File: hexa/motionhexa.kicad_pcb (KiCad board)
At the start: 2 copper layers, 64 x 55.4 mm, 173 parts, among them J1 Conn_01x13_Socket, J2 Conn_01x13_Socket

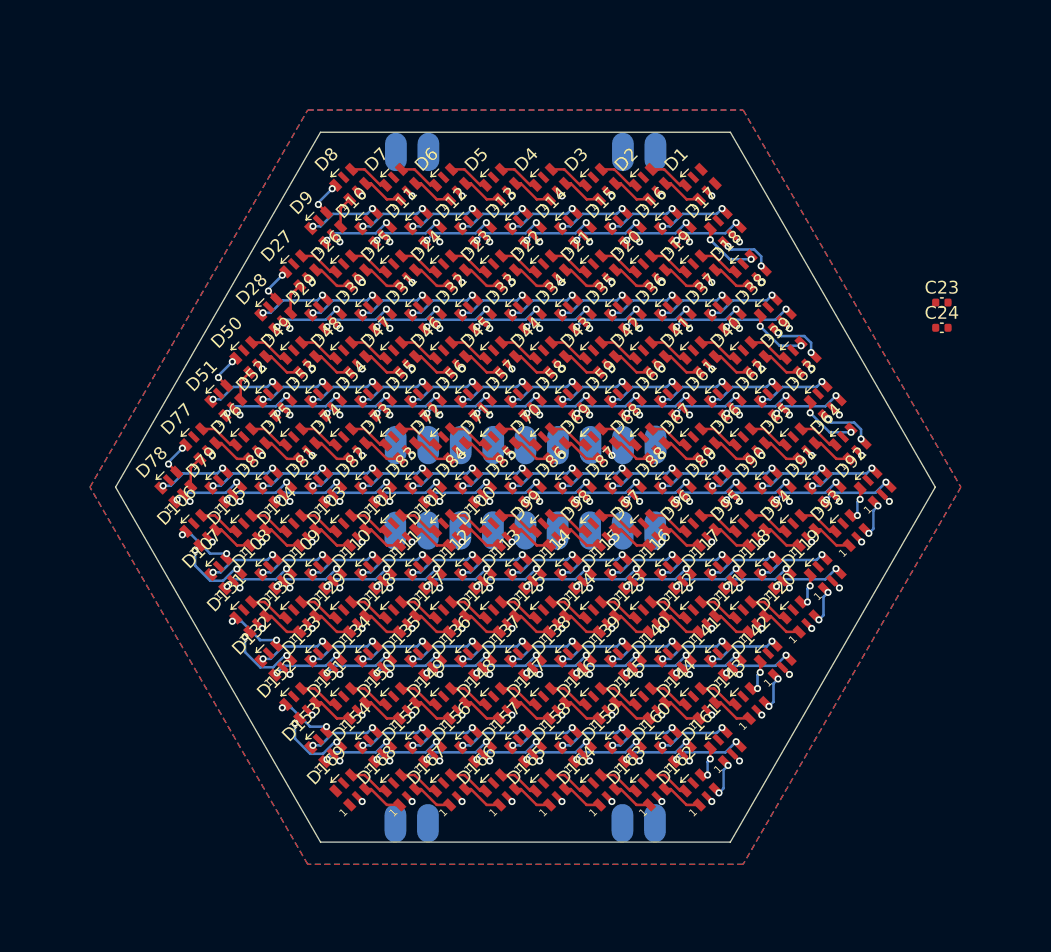
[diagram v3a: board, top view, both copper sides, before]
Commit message: flip direction of pixel data flow and redo all the traces; improvements to layout script including using TraceBuilder for gnd and power draws, and a --lock cli option
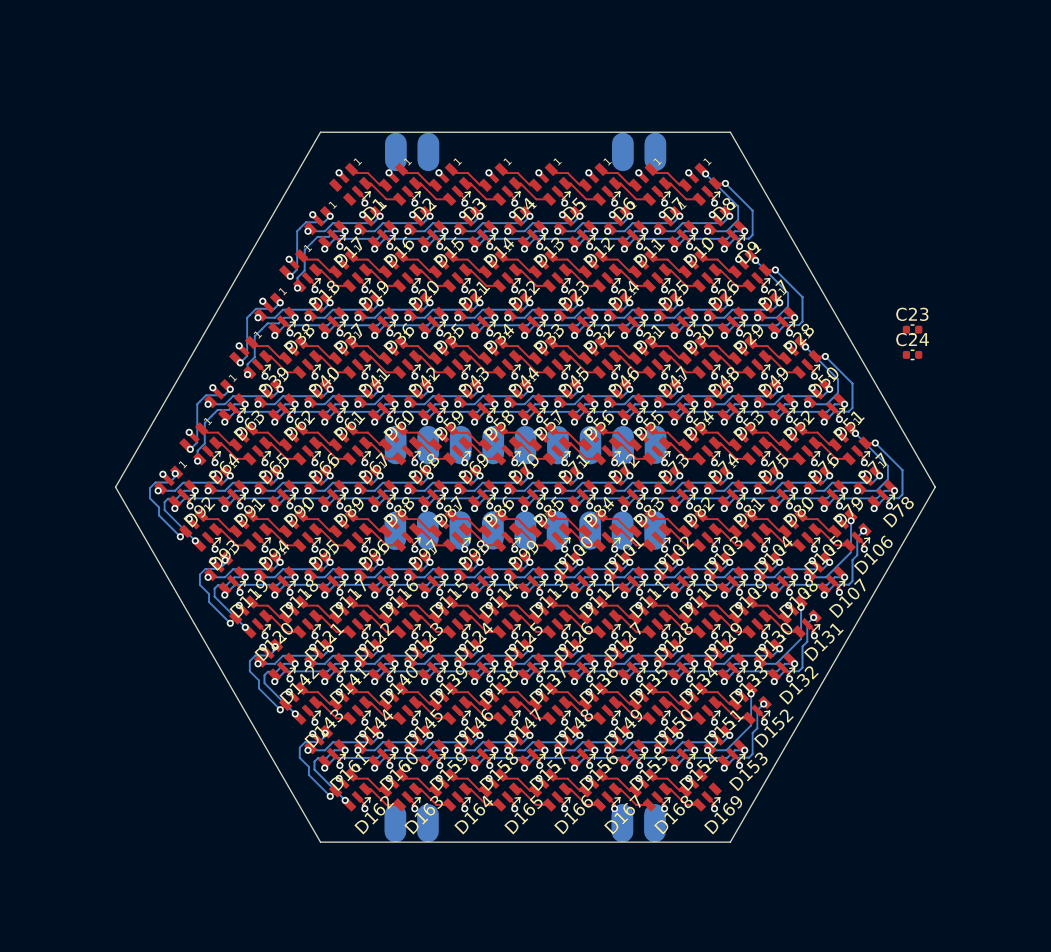
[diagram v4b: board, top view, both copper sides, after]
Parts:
- moved D78 54.6 mm to (127.3, 100.0), turned to 45 degrees
- moved D92 54.6 mm to (72.7, 100.0), turned to 45 degrees
- moved D106 50.7 mm to (125.3, 103.4), turned to 45 degrees
- moved D64 50.7 mm to (74.7, 96.6), turned to 45 degrees
- moved D77 50.7 mm to (125.3, 96.6), turned to 45 degrees
- moved D93 50.7 mm to (74.7, 103.4), turned to 45 degrees
- moved D107 46.8 mm to (123.4, 106.8), turned to 45 degrees
- moved D119 46.8 mm to (76.6, 106.8), turned to 45 degrees
- moved D51 46.8 mm to (123.4, 93.2), turned to 45 degrees
- moved D63 46.8 mm to (76.6, 93.2), turned to 45 degrees
- moved D79 46.8 mm to (123.4, 100.0), turned to 45 degrees
- moved D91 46.8 mm to (76.6, 100.0), turned to 45 degrees
- moved D105 42.9 mm to (121.5, 103.4), turned to 45 degrees
- moved D131 42.9 mm to (121.5, 110.1), turned to 45 degrees
- moved D50 42.9 mm to (121.5, 89.9), turned to 45 degrees
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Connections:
- D1 pad 1: (no net) -> Net-(D1-SDO)
- D1 pad 3: (no net) -> SPI_TX
- D1 pad 4: (no net) -> SPI_SCK
- D1 pad 6: (no net) -> Net-(D1-CKO)
- D10 pad 1: (no net) -> Net-(D10-SDO)
- D10 pad 6: (no net) -> Net-(D10-CKO)
- D100 pad 1: (no net) -> Net-(D100-SDO)
- D100 pad 6: (no net) -> Net-(D100-CKO)
- D101 pad 1: (no net) -> Net-(D101-SDO)
- D101 pad 6: (no net) -> Net-(D101-CKO)
- D102 pad 1: (no net) -> Net-(D102-SDO)
- D102 pad 6: (no net) -> Net-(D102-CKO)
- D103 pad 1: (no net) -> Net-(D103-SDO)
- D103 pad 6: (no net) -> Net-(D103-CKO)
- D104 pad 1: (no net) -> Net-(D104-SDO)
- D104 pad 6: (no net) -> Net-(D104-CKO)
- D105 pad 1: (no net) -> Net-(D105-SDO)
- D105 pad 6: (no net) -> Net-(D105-CKO)
- D106 pad 1: (no net) -> Net-(D106-SDO)
- D106 pad 6: (no net) -> Net-(D106-CKO)
- D107 pad 1: (no net) -> Net-(D107-SDO)
- D107 pad 6: (no net) -> Net-(D107-CKO)
- D108 pad 1: (no net) -> Net-(D108-SDO)
- D108 pad 6: (no net) -> Net-(D108-CKO)
- D109 pad 1: (no net) -> Net-(D109-SDO)
- D109 pad 6: (no net) -> Net-(D109-CKO)
- D11 pad 1: (no net) -> Net-(D11-SDO)
- D11 pad 6: (no net) -> Net-(D11-CKO)
- D110 pad 1: (no net) -> Net-(D110-SDO)
- D110 pad 6: (no net) -> Net-(D110-CKO)
- D111 pad 1: (no net) -> Net-(D111-SDO)
- D111 pad 6: (no net) -> Net-(D111-CKO)
- D112 pad 1: (no net) -> Net-(D112-SDO)
- D112 pad 6: (no net) -> Net-(D112-CKO)
- D113 pad 1: (no net) -> Net-(D113-SDO)
- D113 pad 6: (no net) -> Net-(D113-CKO)
- D114 pad 1: (no net) -> Net-(D114-SDO)
- D114 pad 6: (no net) -> Net-(D114-CKO)
- D115 pad 1: (no net) -> Net-(D115-SDO)
- D115 pad 6: (no net) -> Net-(D115-CKO)
- D116 pad 1: (no net) -> Net-(D116-SDO)
- D116 pad 6: (no net) -> Net-(D116-CKO)
- D117 pad 1: (no net) -> Net-(D117-SDO)
- D117 pad 6: (no net) -> Net-(D117-CKO)
- D118 pad 1: (no net) -> Net-(D118-SDO)
- D118 pad 6: (no net) -> Net-(D118-CKO)
- D119 pad 1: (no net) -> Net-(D119-SDO)
- D119 pad 6: (no net) -> Net-(D119-CKO)
- D12 pad 1: (no net) -> Net-(D12-SDO)
- D12 pad 6: (no net) -> Net-(D12-CKO)
- D120 pad 1: (no net) -> Net-(D120-SDO)
- D120 pad 6: (no net) -> Net-(D120-CKO)
- D121 pad 1: (no net) -> Net-(D121-SDO)
- D121 pad 6: (no net) -> Net-(D121-CKO)
- D122 pad 1: (no net) -> Net-(D122-SDO)
- D122 pad 6: (no net) -> Net-(D122-CKO)
- D123 pad 1: (no net) -> Net-(D123-SDO)
- D123 pad 6: (no net) -> Net-(D123-CKO)
- D124 pad 1: (no net) -> Net-(D124-SDO)
- D124 pad 6: (no net) -> Net-(D124-CKO)
- D125 pad 1: (no net) -> Net-(D125-SDO)
- D125 pad 6: (no net) -> Net-(D125-CKO)
- D126 pad 1: (no net) -> Net-(D126-SDO)
- D126 pad 6: (no net) -> Net-(D126-CKO)
- D127 pad 1: (no net) -> Net-(D127-SDO)
- D127 pad 6: (no net) -> Net-(D127-CKO)
- D128 pad 1: (no net) -> Net-(D128-SDO)
- D128 pad 6: (no net) -> Net-(D128-CKO)
- D129 pad 1: (no net) -> Net-(D129-SDO)
- D129 pad 6: (no net) -> Net-(D129-CKO)
- D13 pad 1: (no net) -> Net-(D13-SDO)
- D13 pad 6: (no net) -> Net-(D13-CKO)
- D130 pad 1: (no net) -> Net-(D130-SDO)
- D130 pad 6: (no net) -> Net-(D130-CKO)
- D131 pad 1: (no net) -> Net-(D131-SDO)
- D131 pad 6: (no net) -> Net-(D131-CKO)
- D132 pad 1: (no net) -> Net-(D132-SDO)
- D132 pad 6: (no net) -> Net-(D132-CKO)
- D133 pad 1: (no net) -> Net-(D133-SDO)
- D133 pad 6: (no net) -> Net-(D133-CKO)
- D134 pad 1: (no net) -> Net-(D134-SDO)
- D134 pad 6: (no net) -> Net-(D134-CKO)
- D135 pad 1: (no net) -> Net-(D135-SDO)
- D135 pad 6: (no net) -> Net-(D135-CKO)
- D136 pad 1: (no net) -> Net-(D136-SDO)
- D136 pad 6: (no net) -> Net-(D136-CKO)
- D137 pad 1: (no net) -> Net-(D137-SDO)
- D137 pad 6: (no net) -> Net-(D137-CKO)
- D138 pad 1: (no net) -> Net-(D138-SDO)
- D138 pad 6: (no net) -> Net-(D138-CKO)
- D139 pad 1: (no net) -> Net-(D139-SDO)
- D139 pad 6: (no net) -> Net-(D139-CKO)
- D14 pad 1: (no net) -> Net-(D14-SDO)
- D14 pad 6: (no net) -> Net-(D14-CKO)
- D140 pad 1: (no net) -> Net-(D140-SDO)
- D140 pad 6: (no net) -> Net-(D140-CKO)
- D141 pad 1: (no net) -> Net-(D141-SDO)
- D141 pad 6: (no net) -> Net-(D141-CKO)
- D142 pad 1: (no net) -> Net-(D142-SDO)
- D142 pad 6: (no net) -> Net-(D142-CKO)
- D143 pad 1: (no net) -> Net-(D143-SDO)
- D143 pad 6: (no net) -> Net-(D143-CKO)
- D144 pad 1: (no net) -> Net-(D144-SDO)
- D144 pad 6: (no net) -> Net-(D144-CKO)
- D145 pad 1: (no net) -> Net-(D145-SDO)
- D145 pad 6: (no net) -> Net-(D145-CKO)
- D146 pad 1: (no net) -> Net-(D146-SDO)
- D146 pad 6: (no net) -> Net-(D146-CKO)
- D147 pad 1: (no net) -> Net-(D147-SDO)
- D147 pad 6: (no net) -> Net-(D147-CKO)
- D148 pad 1: (no net) -> Net-(D148-SDO)
- D148 pad 6: (no net) -> Net-(D148-CKO)
- D149 pad 1: (no net) -> Net-(D149-SDO)
- D149 pad 6: (no net) -> Net-(D149-CKO)
- D15 pad 1: (no net) -> Net-(D15-SDO)
- D15 pad 6: (no net) -> Net-(D15-CKO)
- D150 pad 1: (no net) -> Net-(D150-SDO)
- D150 pad 6: (no net) -> Net-(D150-CKO)
- D151 pad 1: (no net) -> Net-(D151-SDO)
- D151 pad 6: (no net) -> Net-(D151-CKO)
- D152 pad 1: (no net) -> Net-(D152-SDO)
- D152 pad 6: (no net) -> Net-(D152-CKO)
- D153 pad 1: (no net) -> Net-(D153-SDO)
- D153 pad 6: (no net) -> Net-(D153-CKO)
- D154 pad 1: (no net) -> Net-(D154-SDO)
- D154 pad 6: (no net) -> Net-(D154-CKO)
- D155 pad 1: (no net) -> Net-(D155-SDO)
- D155 pad 6: (no net) -> Net-(D155-CKO)
- D156 pad 1: (no net) -> Net-(D156-SDO)
- D156 pad 6: (no net) -> Net-(D156-CKO)
- D157 pad 1: (no net) -> Net-(D157-SDO)
- D157 pad 6: (no net) -> Net-(D157-CKO)
- D158 pad 1: (no net) -> Net-(D158-SDO)
- D158 pad 6: (no net) -> Net-(D158-CKO)
- D159 pad 1: (no net) -> Net-(D159-SDO)
- D159 pad 6: (no net) -> Net-(D159-CKO)
- D16 pad 1: (no net) -> Net-(D16-SDO)
- D16 pad 6: (no net) -> Net-(D16-CKO)
- D160 pad 1: (no net) -> Net-(D160-SDO)
- D160 pad 6: (no net) -> Net-(D160-CKO)
- D161 pad 1: (no net) -> Net-(D161-SDO)
- D161 pad 6: (no net) -> Net-(D161-CKO)
- D162 pad 1: (no net) -> Net-(D162-SDO)
- D162 pad 6: (no net) -> Net-(D162-CKO)
- D163 pad 1: (no net) -> Net-(D163-SDO)
- D163 pad 6: (no net) -> Net-(D163-CKO)
- D164 pad 1: (no net) -> Net-(D164-SDO)
- D164 pad 6: (no net) -> Net-(D164-CKO)
- D165 pad 1: (no net) -> Net-(D165-SDO)
- D165 pad 6: (no net) -> Net-(D165-CKO)
- D166 pad 1: (no net) -> Net-(D166-SDO)
- D166 pad 6: (no net) -> Net-(D166-CKO)
- D167 pad 1: (no net) -> Net-(D167-SDO)
- D167 pad 6: (no net) -> Net-(D167-CKO)
- D168 pad 1: (no net) -> Net-(D168-SDO)
- D168 pad 6: (no net) -> Net-(D168-CKO)
- D169 pad 1: (no net) -> unconnected-(D169-SDO-Pad1)
- D169 pad 6: (no net) -> unconnected-(D169-CKO-Pad6)
- D17 pad 1: (no net) -> Net-(D17-SDO)
- D17 pad 6: (no net) -> Net-(D17-CKO)
- D18 pad 1: (no net) -> Net-(D18-SDO)
- D18 pad 6: (no net) -> Net-(D18-CKO)
- D19 pad 1: (no net) -> Net-(D19-SDO)
- D19 pad 6: (no net) -> Net-(D19-CKO)
- D2 pad 1: (no net) -> Net-(D2-SDO)
- D2 pad 6: (no net) -> Net-(D2-CKO)
- D20 pad 1: (no net) -> Net-(D20-SDO)
- D20 pad 6: (no net) -> Net-(D20-CKO)
- D21 pad 1: (no net) -> Net-(D21-SDO)
- D21 pad 6: (no net) -> Net-(D21-CKO)
- D22 pad 1: (no net) -> Net-(D22-SDO)
- D22 pad 6: (no net) -> Net-(D22-CKO)
- D23 pad 1: (no net) -> Net-(D23-SDO)
- D23 pad 6: (no net) -> Net-(D23-CKO)
- D24 pad 1: (no net) -> Net-(D24-SDO)
- D24 pad 6: (no net) -> Net-(D24-CKO)
- D25 pad 1: (no net) -> Net-(D25-SDO)
- D25 pad 6: (no net) -> Net-(D25-CKO)
- D26 pad 1: (no net) -> Net-(D26-SDO)
- D26 pad 6: (no net) -> Net-(D26-CKO)
- D27 pad 1: (no net) -> Net-(D27-SDO)
- D27 pad 6: (no net) -> Net-(D27-CKO)
- D28 pad 1: (no net) -> Net-(D28-SDO)
- D28 pad 6: (no net) -> Net-(D28-CKO)
- D29 pad 1: (no net) -> Net-(D29-SDO)
- D29 pad 6: (no net) -> Net-(D29-CKO)
- D3 pad 1: (no net) -> Net-(D3-SDO)
- D3 pad 6: (no net) -> Net-(D3-CKO)
- D30 pad 1: (no net) -> Net-(D30-SDO)
- D30 pad 6: (no net) -> Net-(D30-CKO)
- D31 pad 1: (no net) -> Net-(D31-SDO)
- D31 pad 6: (no net) -> Net-(D31-CKO)
- D32 pad 1: (no net) -> Net-(D32-SDO)
- D32 pad 6: (no net) -> Net-(D32-CKO)
- D33 pad 1: (no net) -> Net-(D33-SDO)
- D33 pad 6: (no net) -> Net-(D33-CKO)
- D34 pad 1: (no net) -> Net-(D34-SDO)
- D34 pad 6: (no net) -> Net-(D34-CKO)
- D35 pad 1: (no net) -> Net-(D35-SDO)
- D35 pad 6: (no net) -> Net-(D35-CKO)
- D36 pad 1: (no net) -> Net-(D36-SDO)
- D36 pad 6: (no net) -> Net-(D36-CKO)
- D37 pad 1: (no net) -> Net-(D37-SDO)
- D37 pad 6: (no net) -> Net-(D37-CKO)
- D38 pad 1: (no net) -> Net-(D38-SDO)
- D38 pad 6: (no net) -> Net-(D38-CKO)
- D39 pad 1: (no net) -> Net-(D39-SDO)
- D39 pad 6: (no net) -> Net-(D39-CKO)
- D4 pad 1: (no net) -> Net-(D4-SDO)
- D4 pad 6: (no net) -> Net-(D4-CKO)
- D40 pad 1: (no net) -> Net-(D40-SDO)
- D40 pad 6: (no net) -> Net-(D40-CKO)
- D41 pad 1: (no net) -> Net-(D41-SDO)
- D41 pad 6: (no net) -> Net-(D41-CKO)
- D42 pad 1: (no net) -> Net-(D42-SDO)
- D42 pad 6: (no net) -> Net-(D42-CKO)
- D43 pad 1: (no net) -> Net-(D43-SDO)
- D43 pad 6: (no net) -> Net-(D43-CKO)
- D44 pad 1: (no net) -> Net-(D44-SDO)
- D44 pad 6: (no net) -> Net-(D44-CKO)
- D45 pad 1: (no net) -> Net-(D45-SDO)
- D45 pad 6: (no net) -> Net-(D45-CKO)
- D46 pad 1: (no net) -> Net-(D46-SDO)
- D46 pad 6: (no net) -> Net-(D46-CKO)
- D47 pad 1: (no net) -> Net-(D47-SDO)
- D47 pad 6: (no net) -> Net-(D47-CKO)
- D48 pad 1: (no net) -> Net-(D48-SDO)
- D48 pad 6: (no net) -> Net-(D48-CKO)
- D49 pad 1: (no net) -> Net-(D49-SDO)
- D49 pad 6: (no net) -> Net-(D49-CKO)
- D5 pad 1: (no net) -> Net-(D5-SDO)
- D5 pad 6: (no net) -> Net-(D5-CKO)
- D50 pad 1: (no net) -> Net-(D50-SDO)
- D50 pad 6: (no net) -> Net-(D50-CKO)
- D51 pad 1: (no net) -> Net-(D51-SDO)
- D51 pad 6: (no net) -> Net-(D51-CKO)
- D52 pad 1: (no net) -> Net-(D52-SDO)
- D52 pad 6: (no net) -> Net-(D52-CKO)
- D53 pad 1: (no net) -> Net-(D53-SDO)
- D53 pad 6: (no net) -> Net-(D53-CKO)
- D54 pad 1: (no net) -> Net-(D54-SDO)
- D54 pad 6: (no net) -> Net-(D54-CKO)
- D55 pad 1: (no net) -> Net-(D55-SDO)
- D55 pad 6: (no net) -> Net-(D55-CKO)
- D56 pad 1: (no net) -> Net-(D56-SDO)
- D56 pad 6: (no net) -> Net-(D56-CKO)
- D57 pad 1: (no net) -> Net-(D57-SDO)
- D57 pad 6: (no net) -> Net-(D57-CKO)
- D58 pad 1: (no net) -> Net-(D58-SDO)
- D58 pad 6: (no net) -> Net-(D58-CKO)
- D59 pad 1: (no net) -> Net-(D59-SDO)
- D59 pad 6: (no net) -> Net-(D59-CKO)
- D6 pad 1: (no net) -> Net-(D6-SDO)
- D6 pad 6: (no net) -> Net-(D6-CKO)
- D60 pad 1: (no net) -> Net-(D60-SDO)
- D60 pad 6: (no net) -> Net-(D60-CKO)
- D61 pad 1: (no net) -> Net-(D61-SDO)
- D61 pad 6: (no net) -> Net-(D61-CKO)
- D62 pad 1: (no net) -> Net-(D62-SDO)
- D62 pad 6: (no net) -> Net-(D62-CKO)
- D63 pad 1: (no net) -> Net-(D63-SDO)
- D63 pad 6: (no net) -> Net-(D63-CKO)
- D64 pad 1: (no net) -> Net-(D64-SDO)
- D64 pad 6: (no net) -> Net-(D64-CKO)
- D65 pad 1: (no net) -> Net-(D65-SDO)
- D65 pad 6: (no net) -> Net-(D65-CKO)
- D66 pad 1: (no net) -> Net-(D66-SDO)
- D66 pad 6: (no net) -> Net-(D66-CKO)
- D67 pad 1: (no net) -> Net-(D67-SDO)
- D67 pad 6: (no net) -> Net-(D67-CKO)
- D68 pad 1: (no net) -> Net-(D68-SDO)
- D68 pad 6: (no net) -> Net-(D68-CKO)
- D69 pad 1: (no net) -> Net-(D69-SDO)
- D69 pad 6: (no net) -> Net-(D69-CKO)
- D7 pad 1: (no net) -> Net-(D7-SDO)
- D7 pad 6: (no net) -> Net-(D7-CKO)
- D70 pad 1: (no net) -> Net-(D70-SDO)
- D70 pad 6: (no net) -> Net-(D70-CKO)
- D71 pad 1: (no net) -> Net-(D71-SDO)
- D71 pad 6: (no net) -> Net-(D71-CKO)
- D72 pad 1: (no net) -> Net-(D72-SDO)
- D72 pad 6: (no net) -> Net-(D72-CKO)
- D73 pad 1: (no net) -> Net-(D73-SDO)
- D73 pad 6: (no net) -> Net-(D73-CKO)
- D74 pad 1: (no net) -> Net-(D74-SDO)
- D74 pad 6: (no net) -> Net-(D74-CKO)
- D75 pad 1: (no net) -> Net-(D75-SDO)
- D75 pad 6: (no net) -> Net-(D75-CKO)
- D76 pad 1: (no net) -> Net-(D76-SDO)
- D76 pad 6: (no net) -> Net-(D76-CKO)
- D77 pad 1: (no net) -> Net-(D77-SDO)
- D77 pad 6: (no net) -> Net-(D77-CKO)
- D78 pad 1: (no net) -> Net-(D78-SDO)
- D78 pad 6: (no net) -> Net-(D78-CKO)
- D79 pad 1: (no net) -> Net-(D79-SDO)
- D79 pad 6: (no net) -> Net-(D79-CKO)
- D8 pad 1: (no net) -> Net-(D8-SDO)
- D8 pad 6: (no net) -> Net-(D8-CKO)
- D80 pad 1: (no net) -> Net-(D80-SDO)
- D80 pad 6: (no net) -> Net-(D80-CKO)
- D81 pad 1: (no net) -> Net-(D81-SDO)
- D81 pad 6: (no net) -> Net-(D81-CKO)
- D82 pad 1: (no net) -> Net-(D82-SDO)
- D82 pad 6: (no net) -> Net-(D82-CKO)
- D83 pad 1: (no net) -> Net-(D83-SDO)
- D83 pad 6: (no net) -> Net-(D83-CKO)
- D84 pad 1: (no net) -> Net-(D84-SDO)
- D84 pad 6: (no net) -> Net-(D84-CKO)
- D85 pad 1: (no net) -> Net-(D85-SDO)
- D85 pad 6: (no net) -> Net-(D85-CKO)
- D86 pad 1: (no net) -> Net-(D86-SDO)
- D86 pad 6: (no net) -> Net-(D86-CKO)
- D87 pad 1: (no net) -> Net-(D87-SDO)
- D87 pad 6: (no net) -> Net-(D87-CKO)
- D88 pad 1: (no net) -> Net-(D88-SDO)
- D88 pad 6: (no net) -> Net-(D88-CKO)
- D89 pad 1: (no net) -> Net-(D89-SDO)
- D89 pad 6: (no net) -> Net-(D89-CKO)
- D9 pad 1: (no net) -> Net-(D10-SDI)
- D9 pad 6: (no net) -> Net-(D10-CKI)
- D90 pad 1: (no net) -> Net-(D90-SDO)
- D90 pad 6: (no net) -> Net-(D90-CKO)
- D91 pad 1: (no net) -> Net-(D91-SDO)
- D91 pad 6: (no net) -> Net-(D91-CKO)
- D92 pad 1: (no net) -> Net-(D92-SDO)
- D92 pad 6: (no net) -> Net-(D92-CKO)
- D93 pad 1: (no net) -> Net-(D93-SDO)
- D93 pad 6: (no net) -> Net-(D93-CKO)
- D94 pad 1: (no net) -> Net-(D94-SDO)
- D94 pad 6: (no net) -> Net-(D94-CKO)
- D95 pad 1: (no net) -> Net-(D95-SDO)
- D95 pad 6: (no net) -> Net-(D95-CKO)
- D96 pad 1: (no net) -> Net-(D96-SDO)
- D96 pad 6: (no net) -> Net-(D96-CKO)
- D97 pad 1: (no net) -> Net-(D97-SDO)
- D97 pad 6: (no net) -> Net-(D97-CKO)
- D98 pad 1: (no net) -> Net-(D98-SDO)
- D98 pad 6: (no net) -> Net-(D98-CKO)
- D99 pad 1: (no net) -> Net-(D100-SDI)
- D99 pad 6: (no net) -> Net-(D100-CKI)
- J1 pad 13: OTG -> GPIO11 <-> OTG
- J2 pad 8: +1V8 -> HOST_VREF
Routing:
- net +5V: track 0.00 -> 182.8 mm, vias 1 -> 159
- net GPIO4 <-> INT: track 0.00 -> 9.21 mm, vias 0 -> 5
- net SCL: track 0.00 -> 8.06 mm, vias 0 -> 4
- net Net-(D86-CKO): track 5.91 -> 0.00 mm, vias 2 -> 0
- net Net-(D84-CKO): track 5.91 -> 0.00 mm, vias 2 -> 0
- net Net-(D82-CKO): track 5.91 -> 0.00 mm, vias 2 -> 0
- net Net-(D27-CKO): track 2.96 -> 8.86 mm
- net Net-(D8-CKO): track 2.96 -> 8.86 mm
- net Net-(D50-CKO): track 2.96 -> 8.86 mm
- net Net-(D77-CKO): track 2.96 -> 8.86 mm
- net Net-(D27-SDO): track 2.44 -> 8.19 mm, vias 0 -> 2
- net Net-(D77-SDO): track 2.44 -> 8.19 mm, vias 0 -> 2
- net Net-(D8-SDO): track 2.44 -> 8.19 mm, vias 0 -> 2
- net Net-(D50-SDO): track 2.44 -> 8.19 mm, vias 0 -> 2
- net Net-(D92-CKO): track 2.73 -> 7.77 mm
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- added copper zone on In1.Cu, net +5V
- added copper zone on In2.Cu, net GND
- removed copper zone on F.Cu, net +5V
- removed copper zone on B.Cu, net GND
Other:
- copper layers 2 -> 4

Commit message: realize I need more space on lipo_parallel to prevent likely emi issues on analog/data lines; this commit is tweaks & comments
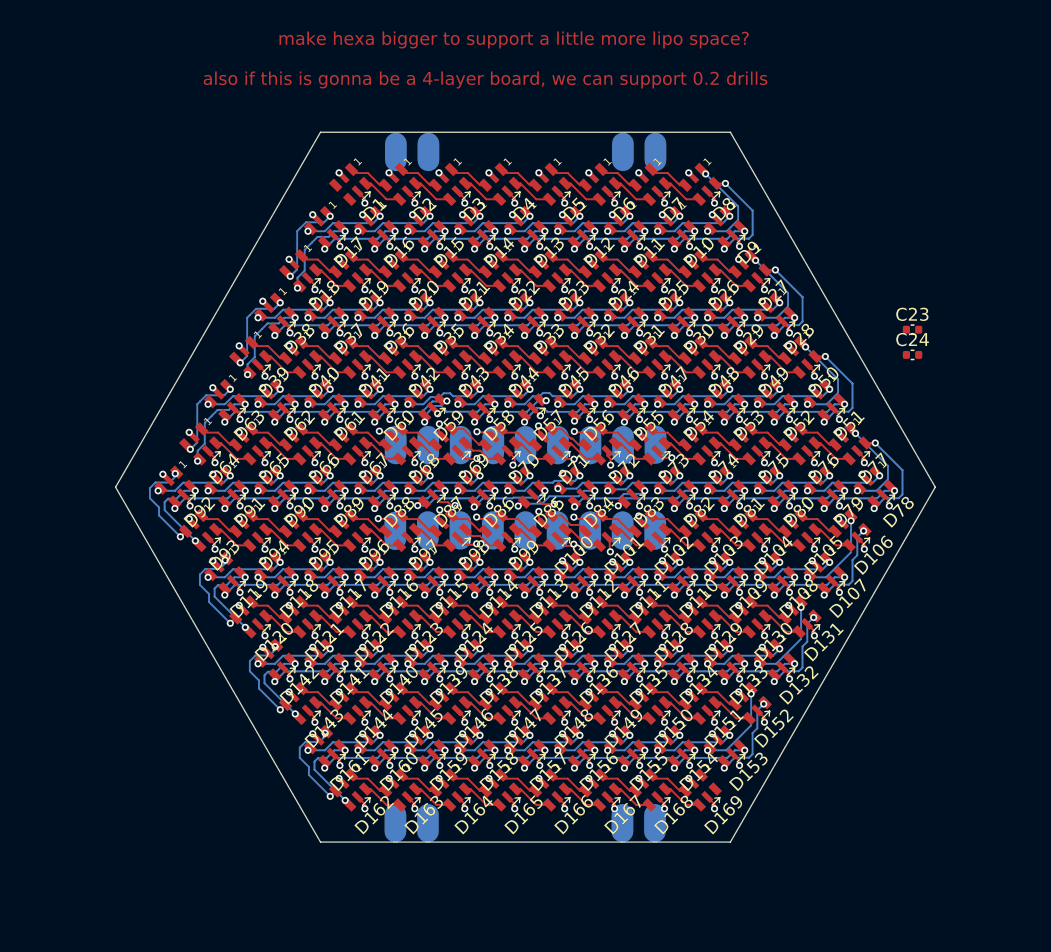
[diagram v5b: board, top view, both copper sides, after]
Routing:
- net +5V: track 182.8 -> 195.9 mm, vias 159 -> 167
- net GPIO4 <-> INT: track 9.21 -> 0.00 mm, vias 5 -> 0
- net SCL: track 8.06 -> 0.00 mm, vias 4 -> 0
- net Net-(D86-CKO): track 0.00 -> 7.67 mm, vias 0 -> 2
- net Net-(D84-CKO): track 0.00 -> 7.61 mm, vias 0 -> 2
- net Net-(D82-CKO): track 0.00 -> 7.56 mm, vias 0 -> 2
- net GND: track 102.8 -> 107.2 mm, vias 164 -> 170
- net SDA: track 2.30 -> 0.00 mm, vias 2 -> 0
- net ADC0 <-> ILIM: track 2.30 -> 0.00 mm, vias 2 -> 0
- net ~{USBBOOT}: track 1.15 -> 0.00 mm, vias 1 -> 0
- net SYS: track 1.00 -> 0.00 mm, vias 2 -> 0
- net HOST_VREF: track 1.00 -> 0.00 mm, vias 2 -> 0
- net GPIO11 <-> OTG: track 1.00 -> 0.00 mm, vias 2 -> 0
- net Net-(D58-CKO): track 7.06 -> 7.73 mm
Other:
- board text added: "also if this is gonna be a 4-layer board, we can support 0.2 drills"
- board text added: "make hexa bigger to support a little more lipo space?"

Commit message: make the lipo_parallel pcb taller to fit everything better; lipo_parallel layout concept for battery terminals on the same side - change pin-matchups to work with that better; make motionhexa larger (more pixels) to accomodate that and bc more pixels = better; insert some capacitors with layout script
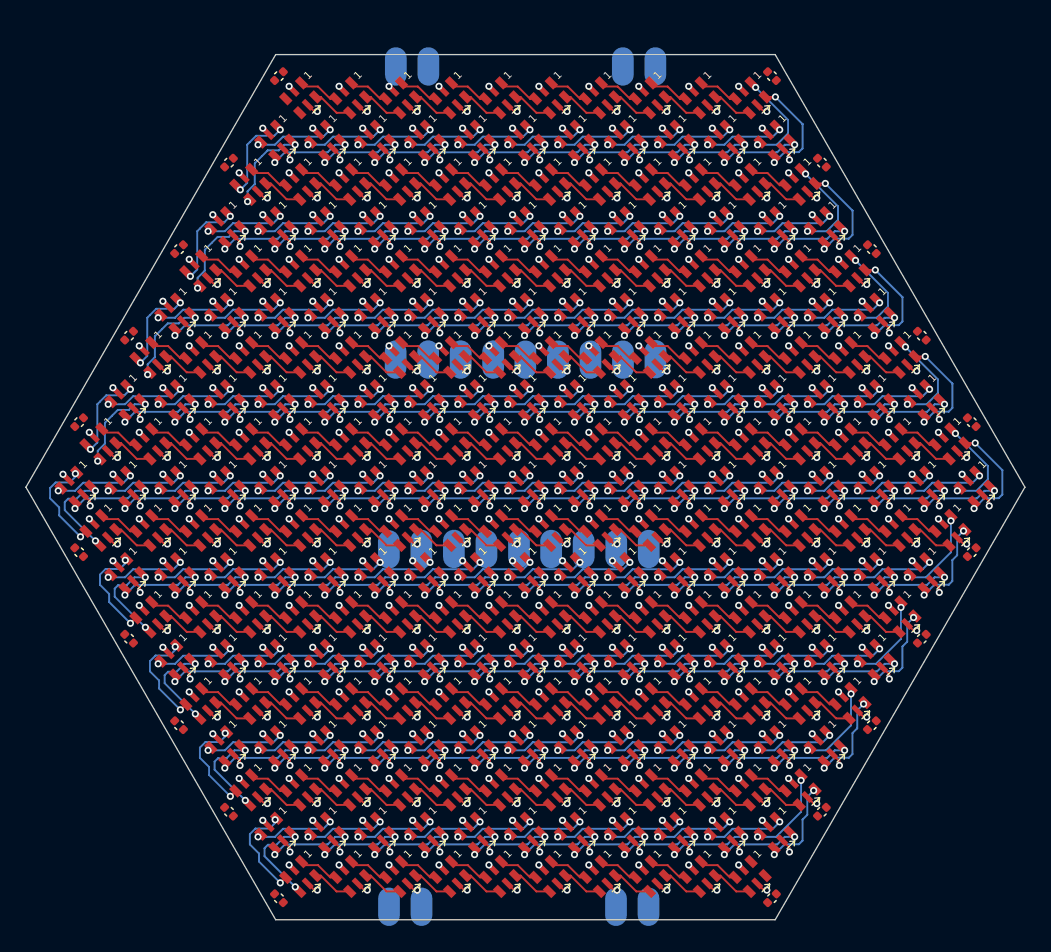
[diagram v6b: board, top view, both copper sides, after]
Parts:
- removed C23, C24: 10u, Capacitor_SMD:C_0402_1005Metric
- added C1: C_0402_1005Metric, C_0402_1005Metric, F.Cu at (80.8, 67.9)
- added C10: C_0402_1005Metric, C_0402_1005Metric, F.Cu at (134.8, 94.9)
- added C11: C_0402_1005Metric, C_0402_1005Metric, F.Cu at (65.2, 105.1)
- added C12: C_0402_1005Metric, C_0402_1005Metric, F.Cu at (134.8, 105.1)
- added C13: C_0402_1005Metric, C_0402_1005Metric, F.Cu at (69.1, 111.8)
- added C14: C_0402_1005Metric, C_0402_1005Metric, F.Cu at (130.9, 111.8)
- added C15: C_0402_1005Metric, C_0402_1005Metric, F.Cu at (73.0, 118.6)
- added C16: C_0402_1005Metric, C_0402_1005Metric, F.Cu at (127.0, 118.6)
- added C17: C_0402_1005Metric, C_0402_1005Metric, F.Cu at (76.9, 125.3)
- added C18: C_0402_1005Metric, C_0402_1005Metric, F.Cu at (123.1, 125.3)
- added C19: C_0402_1005Metric, C_0402_1005Metric, F.Cu at (80.8, 132.1)
- added C2: C_0402_1005Metric, C_0402_1005Metric, F.Cu at (119.2, 67.9)
- added C20: C_0402_1005Metric, C_0402_1005Metric, F.Cu at (119.2, 132.1)
- added C3: C_0402_1005Metric, C_0402_1005Metric, F.Cu at (76.9, 74.7)
- added C4: C_0402_1005Metric, C_0402_1005Metric, F.Cu at (123.1, 74.7)
- added C5: C_0402_1005Metric, C_0402_1005Metric, F.Cu at (73.0, 81.4)
- added C6: C_0402_1005Metric, C_0402_1005Metric, F.Cu at (127.0, 81.4)
- added C7: C_0402_1005Metric, C_0402_1005Metric, F.Cu at (69.1, 88.2)
- added C8: C_0402_1005Metric, C_0402_1005Metric, F.Cu at (130.9, 88.2)
- added C9: C_0402_1005Metric, C_0402_1005Metric, F.Cu at (65.2, 94.9)
- added D170: LED-SK9822-EC20, LED-SK9822-EC20, F.Cu at (107.8, 106.8)
- added D171: LED-SK9822-EC20, LED-SK9822-EC20, F.Cu at (103.9, 106.8)
- added D172: LED-SK9822-EC20, LED-SK9822-EC20, F.Cu at (100.0, 106.8)
- added D173: LED-SK9822-EC20, LED-SK9822-EC20, F.Cu at (96.1, 106.8)
- added D174: LED-SK9822-EC20, LED-SK9822-EC20, F.Cu at (92.2, 106.8)
- added D175: LED-SK9822-EC20, LED-SK9822-EC20, F.Cu at (88.3, 106.8)
- added D176: LED-SK9822-EC20, LED-SK9822-EC20, F.Cu at (84.4, 106.8)
- added D177: LED-SK9822-EC20, LED-SK9822-EC20, F.Cu at (80.5, 106.8)
- added D178: LED-SK9822-EC20, LED-SK9822-EC20, F.Cu at (76.6, 106.8)
- added D179: LED-SK9822-EC20, LED-SK9822-EC20, F.Cu at (72.7, 106.8)
- added D180: LED-SK9822-EC20, LED-SK9822-EC20, F.Cu at (68.8, 106.8)
- added D181: LED-SK9822-EC20, LED-SK9822-EC20, F.Cu at (70.8, 110.1)
- added D182: LED-SK9822-EC20, LED-SK9822-EC20, F.Cu at (74.7, 110.1)
- added D183: LED-SK9822-EC20, LED-SK9822-EC20, F.Cu at (78.5, 110.1)
- added D184: LED-SK9822-EC20, LED-SK9822-EC20, F.Cu at (82.5, 110.1)
- added D185: LED-SK9822-EC20, LED-SK9822-EC20, F.Cu at (86.3, 110.1)
- added D186: LED-SK9822-EC20, LED-SK9822-EC20, F.Cu at (90.2, 110.1)
- added D187: LED-SK9822-EC20, LED-SK9822-EC20, F.Cu at (94.2, 110.1)
- added D188: LED-SK9822-EC20, LED-SK9822-EC20, F.Cu at (98.0, 110.1)
- added D189: LED-SK9822-EC20, LED-SK9822-EC20, F.Cu at (102.0, 110.1)
- added D190: LED-SK9822-EC20, LED-SK9822-EC20, F.Cu at (105.8, 110.1)
- added D191: LED-SK9822-EC20, LED-SK9822-EC20, F.Cu at (109.8, 110.1)
- added D192: LED-SK9822-EC20, LED-SK9822-EC20, F.Cu at (113.7, 110.1)
- added D193: LED-SK9822-EC20, LED-SK9822-EC20, F.Cu at (117.5, 110.1)
- added D194: LED-SK9822-EC20, LED-SK9822-EC20, F.Cu at (121.5, 110.1)
- added D195: LED-SK9822-EC20, LED-SK9822-EC20, F.Cu at (125.3, 110.1)
- added D196: LED-SK9822-EC20, LED-SK9822-EC20, F.Cu at (129.2, 110.1)
- added D197: LED-SK9822-EC20, LED-SK9822-EC20, F.Cu at (127.3, 113.5)
- added D198: LED-SK9822-EC20, LED-SK9822-EC20, F.Cu at (123.4, 113.5)
- added D199: LED-SK9822-EC20, LED-SK9822-EC20, F.Cu at (119.5, 113.5)
- added D200: LED-SK9822-EC20, LED-SK9822-EC20, F.Cu at (115.6, 113.5)
- added D201: LED-SK9822-EC20, LED-SK9822-EC20, F.Cu at (111.7, 113.5)
- added D202: LED-SK9822-EC20, LED-SK9822-EC20, F.Cu at (107.8, 113.5)
- added D203: LED-SK9822-EC20, LED-SK9822-EC20, F.Cu at (103.9, 113.5)
- added D204: LED-SK9822-EC20, LED-SK9822-EC20, F.Cu at (100.0, 113.5)
- added D205: LED-SK9822-EC20, LED-SK9822-EC20, F.Cu at (96.1, 113.5)
- added D206: LED-SK9822-EC20, LED-SK9822-EC20, F.Cu at (92.2, 113.5)
- added D207: LED-SK9822-EC20, LED-SK9822-EC20, F.Cu at (88.3, 113.5)
- added D208: LED-SK9822-EC20, LED-SK9822-EC20, F.Cu at (84.4, 113.5)
- added D209: LED-SK9822-EC20, LED-SK9822-EC20, F.Cu at (80.5, 113.5)
- added D210: LED-SK9822-EC20, LED-SK9822-EC20, F.Cu at (76.6, 113.5)
- added D211: LED-SK9822-EC20, LED-SK9822-EC20, F.Cu at (72.7, 113.5)
- added D212: LED-SK9822-EC20, LED-SK9822-EC20, F.Cu at (74.7, 116.9)
- added D213: LED-SK9822-EC20, LED-SK9822-EC20, F.Cu at (78.5, 116.9)
- added D214: LED-SK9822-EC20, LED-SK9822-EC20, F.Cu at (82.5, 116.9)
- added D215: LED-SK9822-EC20, LED-SK9822-EC20, F.Cu at (86.3, 116.9)
- added D216: LED-SK9822-EC20, LED-SK9822-EC20, F.Cu at (90.2, 116.9)
- added D217: LED-SK9822-EC20, LED-SK9822-EC20, F.Cu at (94.2, 116.9)
- added D218: LED-SK9822-EC20, LED-SK9822-EC20, F.Cu at (98.0, 116.9)
- added D219: LED-SK9822-EC20, LED-SK9822-EC20, F.Cu at (102.0, 116.9)
- added D220: LED-SK9822-EC20, LED-SK9822-EC20, F.Cu at (105.8, 116.9)
- added D221: LED-SK9822-EC20, LED-SK9822-EC20, F.Cu at (109.8, 116.9)
- added D222: LED-SK9822-EC20, LED-SK9822-EC20, F.Cu at (113.7, 116.9)
- added D223: LED-SK9822-EC20, LED-SK9822-EC20, F.Cu at (117.5, 116.9)
- added D224: LED-SK9822-EC20, LED-SK9822-EC20, F.Cu at (121.5, 116.9)
- added D225: LED-SK9822-EC20, LED-SK9822-EC20, F.Cu at (125.3, 116.9)
- added D226: LED-SK9822-EC20, LED-SK9822-EC20, F.Cu at (123.4, 120.3)
- added D227: LED-SK9822-EC20, LED-SK9822-EC20, F.Cu at (119.5, 120.3)
- added D228: LED-SK9822-EC20, LED-SK9822-EC20, F.Cu at (115.6, 120.3)
- added D229: LED-SK9822-EC20, LED-SK9822-EC20, F.Cu at (111.7, 120.3)
- added D230: LED-SK9822-EC20, LED-SK9822-EC20, F.Cu at (107.8, 120.3)
- added D231: LED-SK9822-EC20, LED-SK9822-EC20, F.Cu at (103.9, 120.3)
- added D232: LED-SK9822-EC20, LED-SK9822-EC20, F.Cu at (100.0, 120.3)
- added D233: LED-SK9822-EC20, LED-SK9822-EC20, F.Cu at (96.1, 120.3)
- added D234: LED-SK9822-EC20, LED-SK9822-EC20, F.Cu at (92.2, 120.3)
- added D235: LED-SK9822-EC20, LED-SK9822-EC20, F.Cu at (88.3, 120.3)
- added D236: LED-SK9822-EC20, LED-SK9822-EC20, F.Cu at (84.4, 120.3)
- added D237: LED-SK9822-EC20, LED-SK9822-EC20, F.Cu at (80.5, 120.3)
- added D238: LED-SK9822-EC20, LED-SK9822-EC20, F.Cu at (76.6, 120.3)
- added D239: LED-SK9822-EC20, LED-SK9822-EC20, F.Cu at (78.5, 123.6)
- added D240: LED-SK9822-EC20, LED-SK9822-EC20, F.Cu at (82.5, 123.6)
- added D241: LED-SK9822-EC20, LED-SK9822-EC20, F.Cu at (86.3, 123.6)
- added D242: LED-SK9822-EC20, LED-SK9822-EC20, F.Cu at (90.2, 123.6)
- added D243: LED-SK9822-EC20, LED-SK9822-EC20, F.Cu at (94.2, 123.6)
- added D244: LED-SK9822-EC20, LED-SK9822-EC20, F.Cu at (98.0, 123.6)
- added D245: LED-SK9822-EC20, LED-SK9822-EC20, F.Cu at (102.0, 123.6)
- added D246: LED-SK9822-EC20, LED-SK9822-EC20, F.Cu at (105.8, 123.6)
- added D247: LED-SK9822-EC20, LED-SK9822-EC20, F.Cu at (109.8, 123.6)
- added D248: LED-SK9822-EC20, LED-SK9822-EC20, F.Cu at (113.7, 123.6)
- added D249: LED-SK9822-EC20, LED-SK9822-EC20, F.Cu at (117.5, 123.6)
- added D250: LED-SK9822-EC20, LED-SK9822-EC20, F.Cu at (121.5, 123.6)
- added D251: LED-SK9822-EC20, LED-SK9822-EC20, F.Cu at (119.5, 127.0)
- added D252: LED-SK9822-EC20, LED-SK9822-EC20, F.Cu at (115.6, 127.0)
- added D253: LED-SK9822-EC20, LED-SK9822-EC20, F.Cu at (111.7, 127.0)
- added D254: LED-SK9822-EC20, LED-SK9822-EC20, F.Cu at (107.8, 127.0)
- added D255: LED-SK9822-EC20, LED-SK9822-EC20, F.Cu at (103.9, 127.0)
- added D256: LED-SK9822-EC20, LED-SK9822-EC20, F.Cu at (100.0, 127.0)
- added D257: LED-SK9822-EC20, LED-SK9822-EC20, F.Cu at (96.1, 127.0)
- added D258: LED-SK9822-EC20, LED-SK9822-EC20, F.Cu at (92.2, 127.0)
- added D259: LED-SK9822-EC20, LED-SK9822-EC20, F.Cu at (88.3, 127.0)
- added D260: LED-SK9822-EC20, LED-SK9822-EC20, F.Cu at (84.4, 127.0)
- added D261: LED-SK9822-EC20, LED-SK9822-EC20, F.Cu at (80.5, 127.0)
- added D262: LED-SK9822-EC20, LED-SK9822-EC20, F.Cu at (82.5, 130.4)
- added D263: LED-SK9822-EC20, LED-SK9822-EC20, F.Cu at (86.3, 130.4)
- added D264: LED-SK9822-EC20, LED-SK9822-EC20, F.Cu at (90.2, 130.4)
- added D265: LED-SK9822-EC20, LED-SK9822-EC20, F.Cu at (94.2, 130.4)
- added D266: LED-SK9822-EC20, LED-SK9822-EC20, F.Cu at (98.0, 130.4)
- added D267: LED-SK9822-EC20, LED-SK9822-EC20, F.Cu at (102.0, 130.4)
- added D268: LED-SK9822-EC20, LED-SK9822-EC20, F.Cu at (105.8, 130.4)
- added D269: LED-SK9822-EC20, LED-SK9822-EC20, F.Cu at (109.8, 130.4)
- added D270: LED-SK9822-EC20, LED-SK9822-EC20, F.Cu at (113.7, 130.4)
- added D271: LED-SK9822-EC20, LED-SK9822-EC20, F.Cu at (117.5, 130.4)
- D1, D10, D100, D101, D102, D103, D104, D105, D106, D107, D108, D109, D11, D110, D111, D112, D113, D114, D115, D116, D117, D118, D119, D12, D120, D121, D122, D123, D124, D125, D126, D127, D128, D129, D13, D130, D131, D132, D133, D134, D135, D136, D137, D138, D139, D14, D140, D141, D142, D143, D144, D145, D146, D147, D148, D149, D15, D150, D151, D152, D153, D154, D155, D156, D157, D158, D159, D16, D160, D161, D162, D163, D164, D165, D166, D167, D168, D169, D17, D18, D19, D2, D20, D21, D22, D23, D24, D25, D26, D27, D28, D29, D3, D30, D31, D32, D33, D34, D35, D36, D37, D38, D39, D4, D40, D41, D42, D43, D44, D45, D46, D47, D48, D49, D5, D50, D51, D52, D53, D54, D55, D56, D57, D58, D59, D6, D60, D61, D62, D63, D64, D65, D66, D67, D68, D69, D7, D70, D71, D72, D73, D74, D75, D76, D77, D78, D79, D8, D80, D81, D82, D83, D84, D85, D86, D87, D88, D89, D9, D90, D91, D92, D93, D94, D95, D96, D97, D98, D99: value SK9822-EC20 -> LED-SK9822-EC20; footprint motionhexa:LED-SK9822-EC20 -> LED-SK9822-EC20
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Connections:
- D1 pad 1: Net-(D1-SDO) -> (no net)
- D1 pad 2: GND -> (no net)
- D1 pad 3: SPI_TX -> (no net)
- D1 pad 4: SPI_SCK -> (no net)
- D1 pad 5: +5V -> (no net)
- D1 pad 6: Net-(D1-CKO) -> (no net)
- D10 pad 1: Net-(D10-SDO) -> (no net)
- D10 pad 2: GND -> (no net)
- D10 pad 3: Net-(D10-SDI) -> (no net)
- D10 pad 4: Net-(D10-CKI) -> (no net)
- D10 pad 5: +5V -> (no net)
- D10 pad 6: Net-(D10-CKO) -> (no net)
- D100 pad 1: Net-(D100-SDO) -> (no net)
- D100 pad 2: GND -> (no net)
- D100 pad 3: Net-(D100-SDI) -> (no net)
- D100 pad 4: Net-(D100-CKI) -> (no net)
- D100 pad 5: +5V -> (no net)
- D100 pad 6: Net-(D100-CKO) -> (no net)
- D101 pad 1: Net-(D101-SDO) -> (no net)
- D101 pad 2: GND -> (no net)
- D101 pad 3: Net-(D100-SDO) -> (no net)
- D101 pad 4: Net-(D100-CKO) -> (no net)
- D101 pad 5: +5V -> (no net)
- D101 pad 6: Net-(D101-CKO) -> (no net)
- D102 pad 1: Net-(D102-SDO) -> (no net)
- D102 pad 2: GND -> (no net)
- D102 pad 3: Net-(D101-SDO) -> (no net)
- D102 pad 4: Net-(D101-CKO) -> (no net)
- D102 pad 5: +5V -> (no net)
- D102 pad 6: Net-(D102-CKO) -> (no net)
- D103 pad 1: Net-(D103-SDO) -> (no net)
- D103 pad 2: GND -> (no net)
- D103 pad 3: Net-(D102-SDO) -> (no net)
- D103 pad 4: Net-(D102-CKO) -> (no net)
- D103 pad 5: +5V -> (no net)
- D103 pad 6: Net-(D103-CKO) -> (no net)
- D104 pad 1: Net-(D104-SDO) -> (no net)
- D104 pad 2: GND -> (no net)
- D104 pad 3: Net-(D103-SDO) -> (no net)
- D104 pad 4: Net-(D103-CKO) -> (no net)
- D104 pad 5: +5V -> (no net)
- D104 pad 6: Net-(D104-CKO) -> (no net)
- D105 pad 1: Net-(D105-SDO) -> (no net)
- D105 pad 2: GND -> (no net)
- D105 pad 3: Net-(D104-SDO) -> (no net)
- D105 pad 4: Net-(D104-CKO) -> (no net)
- D105 pad 5: +5V -> (no net)
- D105 pad 6: Net-(D105-CKO) -> (no net)
- D106 pad 1: Net-(D106-SDO) -> (no net)
- D106 pad 2: GND -> (no net)
- D106 pad 3: Net-(D105-SDO) -> (no net)
- D106 pad 4: Net-(D105-CKO) -> (no net)
- D106 pad 5: +5V -> (no net)
- D106 pad 6: Net-(D106-CKO) -> (no net)
- D107 pad 1: Net-(D107-SDO) -> (no net)
- D107 pad 2: GND -> (no net)
- D107 pad 3: Net-(D106-SDO) -> (no net)
- D107 pad 4: Net-(D106-CKO) -> (no net)
- D107 pad 5: +5V -> (no net)
- D107 pad 6: Net-(D107-CKO) -> (no net)
- D108 pad 1: Net-(D108-SDO) -> (no net)
- D108 pad 2: GND -> (no net)
- D108 pad 3: Net-(D107-SDO) -> (no net)
- D108 pad 4: Net-(D107-CKO) -> (no net)
- D108 pad 5: +5V -> (no net)
- D108 pad 6: Net-(D108-CKO) -> (no net)
- D109 pad 1: Net-(D109-SDO) -> (no net)
- D109 pad 2: GND -> (no net)
- D109 pad 3: Net-(D108-SDO) -> (no net)
- D109 pad 4: Net-(D108-CKO) -> (no net)
- D109 pad 5: +5V -> (no net)
- D109 pad 6: Net-(D109-CKO) -> (no net)
- D11 pad 1: Net-(D11-SDO) -> (no net)
- D11 pad 2: GND -> (no net)
- D11 pad 3: Net-(D10-SDO) -> (no net)
- D11 pad 4: Net-(D10-CKO) -> (no net)
- D11 pad 5: +5V -> (no net)
- D11 pad 6: Net-(D11-CKO) -> (no net)
- D110 pad 1: Net-(D110-SDO) -> (no net)
- D110 pad 2: GND -> (no net)
- D110 pad 3: Net-(D109-SDO) -> (no net)
- D110 pad 4: Net-(D109-CKO) -> (no net)
- D110 pad 5: +5V -> (no net)
- D110 pad 6: Net-(D110-CKO) -> (no net)
- D111 pad 1: Net-(D111-SDO) -> (no net)
- D111 pad 2: GND -> (no net)
- D111 pad 3: Net-(D110-SDO) -> (no net)
- D111 pad 4: Net-(D110-CKO) -> (no net)
- D111 pad 5: +5V -> (no net)
- D111 pad 6: Net-(D111-CKO) -> (no net)
- D112 pad 1: Net-(D112-SDO) -> (no net)
- D112 pad 2: GND -> (no net)
- D112 pad 3: Net-(D111-SDO) -> (no net)
- D112 pad 4: Net-(D111-CKO) -> (no net)
- D112 pad 5: +5V -> (no net)
- D112 pad 6: Net-(D112-CKO) -> (no net)
- D113 pad 1: Net-(D113-SDO) -> (no net)
- D113 pad 2: GND -> (no net)
- D113 pad 3: Net-(D112-SDO) -> (no net)
- D113 pad 4: Net-(D112-CKO) -> (no net)
- D113 pad 5: +5V -> (no net)
- D113 pad 6: Net-(D113-CKO) -> (no net)
- D114 pad 1: Net-(D114-SDO) -> (no net)
- D114 pad 2: GND -> (no net)
- D114 pad 3: Net-(D113-SDO) -> (no net)
- D114 pad 4: Net-(D113-CKO) -> (no net)
- D114 pad 5: +5V -> (no net)
- D114 pad 6: Net-(D114-CKO) -> (no net)
- D115 pad 1: Net-(D115-SDO) -> (no net)
- D115 pad 2: GND -> (no net)
- D115 pad 3: Net-(D114-SDO) -> (no net)
- D115 pad 4: Net-(D114-CKO) -> (no net)
- D115 pad 5: +5V -> (no net)
- D115 pad 6: Net-(D115-CKO) -> (no net)
- D116 pad 1: Net-(D116-SDO) -> (no net)
- D116 pad 2: GND -> (no net)
- D116 pad 3: Net-(D115-SDO) -> (no net)
- D116 pad 4: Net-(D115-CKO) -> (no net)
- D116 pad 5: +5V -> (no net)
- D116 pad 6: Net-(D116-CKO) -> (no net)
- D117 pad 1: Net-(D117-SDO) -> (no net)
- D117 pad 2: GND -> (no net)
- D117 pad 3: Net-(D116-SDO) -> (no net)
- D117 pad 4: Net-(D116-CKO) -> (no net)
- D117 pad 5: +5V -> (no net)
- D117 pad 6: Net-(D117-CKO) -> (no net)
- D118 pad 1: Net-(D118-SDO) -> (no net)
- D118 pad 2: GND -> (no net)
- D118 pad 3: Net-(D117-SDO) -> (no net)
- D118 pad 4: Net-(D117-CKO) -> (no net)
- D118 pad 5: +5V -> (no net)
- D118 pad 6: Net-(D118-CKO) -> (no net)
- D119 pad 1: Net-(D119-SDO) -> (no net)
- D119 pad 2: GND -> (no net)
- D119 pad 3: Net-(D118-SDO) -> (no net)
- D119 pad 4: Net-(D118-CKO) -> (no net)
- D119 pad 5: +5V -> (no net)
- D119 pad 6: Net-(D119-CKO) -> (no net)
- D12 pad 1: Net-(D12-SDO) -> (no net)
- D12 pad 2: GND -> (no net)
- D12 pad 3: Net-(D11-SDO) -> (no net)
- D12 pad 4: Net-(D11-CKO) -> (no net)
- D12 pad 5: +5V -> (no net)
- D12 pad 6: Net-(D12-CKO) -> (no net)
- D120 pad 1: Net-(D120-SDO) -> (no net)
- D120 pad 2: GND -> (no net)
- D120 pad 3: Net-(D119-SDO) -> (no net)
- D120 pad 4: Net-(D119-CKO) -> (no net)
- D120 pad 5: +5V -> (no net)
- D120 pad 6: Net-(D120-CKO) -> (no net)
- D121 pad 1: Net-(D121-SDO) -> (no net)
- D121 pad 2: GND -> (no net)
- D121 pad 3: Net-(D120-SDO) -> (no net)
- D121 pad 4: Net-(D120-CKO) -> (no net)
- D121 pad 5: +5V -> (no net)
- D121 pad 6: Net-(D121-CKO) -> (no net)
- D122 pad 1: Net-(D122-SDO) -> (no net)
- D122 pad 2: GND -> (no net)
- D122 pad 3: Net-(D121-SDO) -> (no net)
- D122 pad 4: Net-(D121-CKO) -> (no net)
- D122 pad 5: +5V -> (no net)
- D122 pad 6: Net-(D122-CKO) -> (no net)
- D123 pad 1: Net-(D123-SDO) -> (no net)
- D123 pad 2: GND -> (no net)
- D123 pad 3: Net-(D122-SDO) -> (no net)
- D123 pad 4: Net-(D122-CKO) -> (no net)
- D123 pad 5: +5V -> (no net)
- D123 pad 6: Net-(D123-CKO) -> (no net)
- D124 pad 1: Net-(D124-SDO) -> (no net)
- D124 pad 2: GND -> (no net)
- D124 pad 3: Net-(D123-SDO) -> (no net)
- D124 pad 4: Net-(D123-CKO) -> (no net)
- D124 pad 5: +5V -> (no net)
- D124 pad 6: Net-(D124-CKO) -> (no net)
- D125 pad 1: Net-(D125-SDO) -> (no net)
- D125 pad 2: GND -> (no net)
- D125 pad 3: Net-(D124-SDO) -> (no net)
- D125 pad 4: Net-(D124-CKO) -> (no net)
- D125 pad 5: +5V -> (no net)
- D125 pad 6: Net-(D125-CKO) -> (no net)
- D126 pad 1: Net-(D126-SDO) -> (no net)
- D126 pad 2: GND -> (no net)
- D126 pad 3: Net-(D125-SDO) -> (no net)
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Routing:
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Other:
- board size 64 x 55.4 mm -> 78 x 67.5 mm
- board text removed: "also if this is gonna be a 4-layer board, we can support 0.2 drills"
- board text removed: "make hexa bigger to support a little more lipo space?"
